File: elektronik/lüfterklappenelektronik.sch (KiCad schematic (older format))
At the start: 96 parts, among them J101 Conn_01x05_Male, J102 Ckmtw_2510S-2P, J103 Conn_LAN_ENC28J60, J104 USB_B_Micro, J105 #Stecker, J106 Ckmtw_2510S-2P, J107 Ckmtw_2510S-2P, J108 Ckmtw_2510S-2P, P101 PWR_BUS_CONN1, P102 #FAN_230VAC_Phase, P103 PressureSensor3, P104 PressureSensor1, P105 PressureSensor2, P109 PWR_BUS_CONN2, Q101 IRLR8743TRPBF, Q102 IRLR8743TRPBF, Q103 IRLR8743TRPBF, Q104 Q_NPN_Darlington_BEC, Q105 Q_NPN_Darlington_BEC, SW101 SW_Push, SW102 SW_Push, U101 Gabellichtschranke, U102 Gabellichtschranke, U103 Gabellichtschranke, U104 #ZG3NC-240B, U105 ESP32-WROOM-32E, U106 AMS1117-3.3, U107 CP2102N-A01-GQFN28

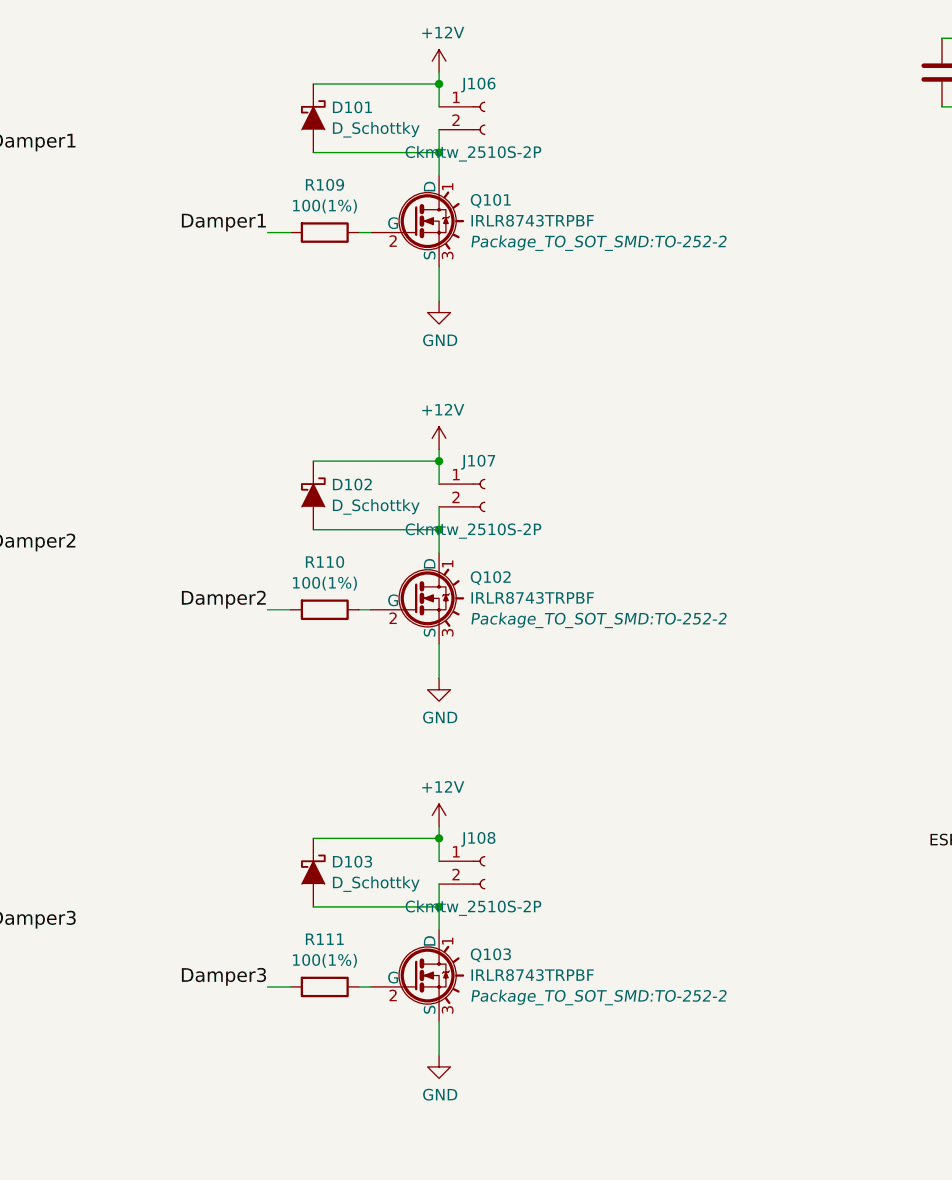
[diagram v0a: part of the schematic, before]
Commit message: place some groups
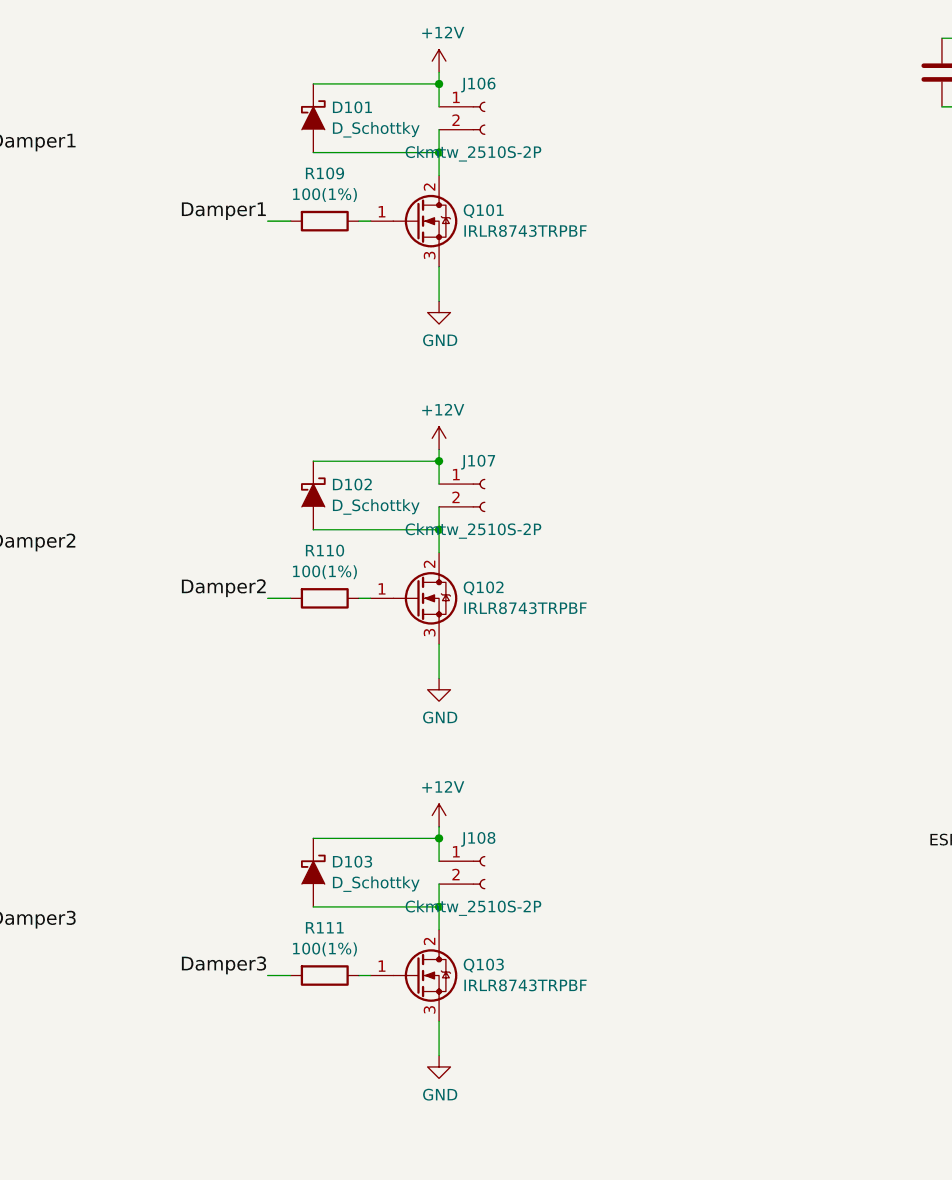
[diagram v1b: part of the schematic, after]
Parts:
- removed Q101, Q102, Q103: IRLR8743TRPBF, Package_TO_SOT_SMD:TO-252-2, symbol lüfterklappenelektronik-rescue:BUZ11
- added Q101, Q102, Q103: IRLR8743TRPBF, Package_TO_SOT_SMD:TO-252-2, symbol Transistor_FET:IRLB8721PBF
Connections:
- net GND: now also Q101.3 (S), Q102.3 (S), Q103.3 (S)
- net at D101.2 (A), J106.2 (Pin_2): now also Q101.2 (D)
- net at R109.1: now also Q101.1 (G)
- net at R110.1: now also Q102.1 (G)
- net at R111.1: now also Q103.1 (G)
- net at D103.2 (A), J108.2 (Pin_2): now also Q103.2 (D)
- net at D102.2 (A), J107.2 (Pin_2): now also Q102.2 (D)
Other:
- moved on the sheet: R109, R110, R111
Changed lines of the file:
@@
 L lüfterklappenelektronik-rescue:R R109
 U 1 1 57419FFE
-P 4450 1850
-F 0 "R109" V 4243 1850 50  0000 C CNN
-F 1 "100(1%)" V 4334 1850 50  0000 C CNN
-F 2 "Resistor_SMD:R_0603_1608Metric" V 4380 1850 50  0001 C CNN
-F 3 "" H 4450 1850 50  0000 C CNN
-	1    4450 1850
-	0    1    1    0
-$EndComp
-Wire Wire Line
-	4600 1850 4650 1850
+P 4450 1800
+F 0 "R109" V 4243 1800 50  0000 C CNN
+F 1 "100(1%)" V 4334 1800 50  0000 C CNN
+F 2 "Resistor_SMD:R_0603_1608Metric" V 4380 1800 50  0001 C CNN
+F 3 "" H 4450 1800 50  0000 C CNN
+	1    4450 1800
+	0    1    1    0
+$EndComp
+Wire Wire Line
+	4600 1800 4650 1800
 $Comp
 L power:GND #PWR02
@@
 	1    0    0    -1
 $EndComp
-Wire Wire Line
-	4950 2000 4950 2150
-Text Label 4200 1850 2    60   ~ 0
+Text Label 4200 1800 2    60   ~ 0
 Damper1
 Wire Wire Line
-	4200 1850 4300 1850
+	4200 1800 4300 1800
 $Comp
 L power:+12V #PWR03
@@
 L lüfterklappenelektronik-rescue:R R110
 U 1 1 5741A896
-P 4450 3500
-F 0 "R110" V 4243 3500 50  0000 C CNN
-F 1 "100(1%)" V 4334 3500 50  0000 C CNN
-F 2 "Resistor_SMD:R_0603_1608Metric" V 4380 3500 50  0001 C CNN
-F 3 "" H 4450 3500 50  0000 C CNN
-	1    4450 3500
-	0    1    1    0
-$EndComp
-Wire Wire Line
-	4600 3500 4650 3500
+P 4450 3450
+F 0 "R110" V 4243 3450 50  0000 C CNN
+F 1 "100(1%)" V 4334 3450 50  0000 C CNN
+F 2 "Resistor_SMD:R_0603_1608Metric" V 4380 3450 50  0001 C CNN
+F 3 "" H 4450 3450 50  0000 C CNN
+	1    4450 3450
+	0    1    1    0
+$EndComp
+Wire Wire Line
+	4600 3450 4650 3450
 $Comp
 L power:GND #PWR04
@@
 Wire Wire Line
 	4950 3650 4950 3800
-Text Label 4200 3500 2    60   ~ 0
+Text Label 4200 3450 2    60   ~ 0
 Damper2
 Wire Wire Line
-	4200 3500 4300 3500
+	4200 3450 4300 3450
 $Comp
 L power:+12V #PWR05
@@
 L lüfterklappenelektronik-rescue:R R111
 U 1 1 5741AA44
-P 4450 5150
-F 0 "R111" V 4243 5150 50  0000 C CNN
-F 1 "100(1%)" V 4334 5150 50  0000 C CNN
-F 2 "Resistor_SMD:R_0603_1608Metric" V 4380 5150 50  0001 C CNN
-F 3 "" H 4450 5150 50  0000 C CNN
-	1    4450 5150
-	0    1    1    0
-$EndComp
-Wire Wire Line
-	4600 5150 4650 5150
+P 4450 5100
+F 0 "R111" V 4243 5100 50  0000 C CNN
+F 1 "100(1%)" V 4334 5100 50  0000 C CNN
+F 2 "Resistor_SMD:R_0603_1608Metric" V 4380 5100 50  0001 C CNN
+F 3 "" H 4450 5100 50  0000 C CNN
+	1    4450 5100
+	0    1    1    0
+$EndComp
+Wire Wire Line
+	4600 5100 4650 5100
 $Comp
 L power:GND #PWR06
@@
 Wire Wire Line
 	4950 5300 4950 5450
-Text Label 4200 5150 2    60   ~ 0
+Text Label 4200 5100 2    60   ~ 0
 Damper3
 Wire Wire Line
-	4200 5150 4300 5150
+	4200 5100 4300 5100
 Text Label 3050 6750 2    60   ~ 0
 FAN
@@
 F 3 "" H 1950 6650 50  0000 C CNN
 	1    1950 6650
-	1    0    0    -1
-$EndComp
-$Comp
-L lüfterklappenelektronik-rescue:BUZ11 Q103
-U 1 1 57544167
-P 4850 5100
-F 0 "Q103" H 5085 5191 50  0000 L CNN
-F 1 "IRLR8743TRPBF" H 5085 5100 50  0000 L CNN
-F 2 "Package_TO_SOT_SMD:TO-252-2" H 5085 5009 50  0000 L CIN
-F 3 "" H 4850 5100 50  0000 L CNN
-	1    4850 5100
-	1    0    0    -1
-$EndComp
-$Comp
-L lüfterklappenelektronik-rescue:BUZ11 Q102
-U 1 1 5754473E
-P 4850 3450
-F 0 "Q102" H 5085 3541 50  0000 L CNN
-F 1 "IRLR8743TRPBF" H 5085 3450 50  0000 L CNN
-F 2 "Package_TO_SOT_SMD:TO-252-2" H 5085 3359 50  0000 L CIN
-F 3 "" H 4850 3450 50  0000 L CNN
-	1    4850 3450
-	1    0    0    -1
-$EndComp
-$Comp
-L lüfterklappenelektronik-rescue:BUZ11 Q101
-U 1 1 575449DD
-P 4850 1800
-F 0 "Q101" H 5085 1891 50  0000 L CNN
-F 1 "IRLR8743TRPBF" H 5085 1800 50  0000 L CNN
-F 2 "Package_TO_SOT_SMD:TO-252-2" H 5085 1709 50  0000 L CIN
-F 3 "https://datasheet.lcsc.com/szlcsc/1809061832_Infineon-Technologies-IRLR8743TRPBF_C51360.pdf" H 4850 1800 50  0001 L CNN
-F 4 "Infineon Technologies" H 4850 1800 50  0001 C CNN "MF"
-F 5 "IRLR8743TRPBF" H 4850 1800 50  0001 C CNN "MP"
-F 6 "LCSC" H 4850 1800 50  0001 C CNN "Distributor"
-F 7 "C51360" H 4850 1800 50  0001 C CNN "LCSCPartN"
-	1    4850 1800
 	1    0    0    -1
 $EndComp
@@
 	1    0    0    -1
 $EndComp
+$Comp
+L Transistor_FET:IRLB8721PBF Q101
+U 1 1 6113C9FF
+P 4850 1800
+F 0 "Q101" H 5054 1846 50  0000 L CNN
+F 1 "IRLR8743TRPBF" H 5054 1755 50  0000 L CNN
+F 2 "Package_TO_SOT_SMD:TO-252-2" H 5100 1725 50  0001 L CIN
+F 3 "https://datasheet.lcsc.com/szlcsc/1809061832_Infineon-Technologies-IRLR8743TRPBF_C51360.pdf" H 4850 1800 50  0001 L CNN
+F 4 "Infineon Technologies" H 4850 1800 50  0001 C CNN "MF"
+F 5 "IRLR8743TRPBF" H 4850 1800 50  0001 C CNN "MP"
+F 6 "LCSC" H 4850 1800 50  0001 C CNN "Distributor"
+F 7 "C51360" H 4850 1800 50  0001 C CNN "LCSCPartN"
+F 8 "SMT" H 4850 1800 50  0001 C CNN "Type"
+	1    4850 1800
+	1    0    0    -1
+$EndComp
+Wire Wire Line
+	4950 2000 4950 2150
+$Comp
+L Transistor_FET:IRLB8721PBF Q102
+U 1 1 6118E7D4
+P 4850 3450
+F 0 "Q102" H 5054 3496 50  0000 L CNN
+F 1 "IRLR8743TRPBF" H 5054 3405 50  0000 L CNN
+F 2 "Package_TO_SOT_SMD:TO-252-2" H 5100 3375 50  0001 L CIN
+F 3 "https://datasheet.lcsc.com/szlcsc/1809061832_Infineon-Technologies-IRLR8743TRPBF_C51360.pdf" H 4850 3450 50  0001 L CNN
+F 4 "Infineon Technologies" H 4850 3450 50  0001 C CNN "MF"
+F 5 "IRLR8743TRPBF" H 4850 3450 50  0001 C CNN "MP"
+F 6 "LCSC" H 4850 3450 50  0001 C CNN "Distributor"
+F 7 "C51360" H 4850 3450 50  0001 C CNN "LCSCPartN"
+F 8 "SMT" H 4850 3450 50  0001 C CNN "Type"
+	1    4850 3450
+	1    0    0    -1
+$EndComp
+$Comp
+L Transistor_FET:IRLB8721PBF Q103
+U 1 1 6118F713
+P 4850 5100
+F 0 "Q103" H 5054 5146 50  0000 L CNN
+F 1 "IRLR8743TRPBF" H 5054 5055 50  0000 L CNN
+F 2 "Package_TO_SOT_SMD:TO-252-2" H 5100 5025 50  0001 L CIN
+F 3 "https://datasheet.lcsc.com/szlcsc/1809061832_Infineon-Technologies-IRLR8743TRPBF_C51360.pdf" H 4850 5100 50  0001 L CNN
+F 4 "Infineon Technologies" H 4850 5100 50  0001 C CNN "MF"
+F 5 "IRLR8743TRPBF" H 4850 5100 50  0001 C CNN "MP"
+F 6 "LCSC" H 4850 5100 50  0001 C CNN "Distributor"
+F 7 "C51360" H 4850 5100 50  0001 C CNN "LCSCPartN"
+F 8 "SMT" H 4850 5100 50  0001 C CNN "Type"
+	1    4850 5100
+	1    0    0    -1
+$EndComp

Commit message: rough placing
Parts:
- J106, J107, J108: value Ckmtw_2510S-2P -> WJ2EDGRC-5.08-2P; footprint Connect:PINHEAD1-2 -> FootprintsTittelbach:WJ2EDGRC-5.08-2P; LCSCPartN C30436 -> C3697; MF BOOMELE(Boom Precision Elec) -> Ningbo Kangnex Elec; MP C30436 -> WJ2EDGRC-5.08-2P
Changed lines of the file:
@@
 F 1 "Gabellichtschranke" H 1750 2034 50  0000 C CNN
 F 2 "FootprintsTittelbach:Ckmtw_2510S-4P" H 1750 1700 50  0001 C CNN
-F 3 "https://datasheet.lcsc.com/szlcsc/1811061121_BOOMELE-Boom-Precision-Elec-C31753_C31753.pdf" H 1750 1700 50  0001 C CNN
+F 3 "https://datasheet.lcsc.com/szlcsc/1806151523_Ckmtw-Shenzhen-Cankemeng-2510S-4P_C140769.pdf" H 1750 1700 50  0001 C CNN
 F 4 "Ckmtw(Shenzhen Cankemeng)" H 1750 1700 50  0001 C CNN "MF"
 F 5 "2510S-4P" H 1750 1700 50  0001 C CNN "MP"
@@
 F 1 "Gabellichtschranke" H 1750 3784 50  0000 C CNN
 F 2 "FootprintsTittelbach:Ckmtw_2510S-4P" H 1750 3450 50  0001 C CNN
-F 3 "https://datasheet.lcsc.com/szlcsc/1811061121_BOOMELE-Boom-Precision-Elec-C31753_C31753.pdf" H 1750 3450 50  0001 C CNN
+F 3 "https://datasheet.lcsc.com/szlcsc/1806151523_Ckmtw-Shenzhen-Cankemeng-2510S-4P_C140769.pdf" H 1750 3450 50  0001 C CNN
 F 4 "Ckmtw(Shenzhen Cankemeng)" H 1750 3450 50  0001 C CNN "MF"
 F 5 "2510S-4P" H 1750 3450 50  0001 C CNN "MP"
@@
 F 1 "Gabellichtschranke" H 1750 5434 50  0000 C CNN
 F 2 "FootprintsTittelbach:Ckmtw_2510S-4P" H 1750 5100 50  0001 C CNN
-F 3 "https://datasheet.lcsc.com/szlcsc/1811061121_BOOMELE-Boom-Precision-Elec-C31753_C31753.pdf" H 1750 5100 50  0001 C CNN
+F 3 "https://datasheet.lcsc.com/szlcsc/1806151523_Ckmtw-Shenzhen-Cankemeng-2510S-4P_C140769.pdf" H 1750 5100 50  0001 C CNN
 F 4 "Ckmtw(Shenzhen Cankemeng)" H 1750 5100 50  0001 C CNN "MF"
 F 5 "2510S-4P" H 1750 5100 50  0001 C CNN "MP"
@@
 P 5150 1300
 F 0 "J106" H 5050 1400 50  0000 L CNN
-F 1 "Ckmtw_2510S-2P" H 4800 1100 50  0000 L CNN
-F 2 "Connect:PINHEAD1-2" H 5150 1300 50  0001 C CNN
-F 3 "~" H 5150 1300 50  0001 C CNN
-F 4 " BOOMELE(Boom Precision Elec) " H 5150 1300 50  0001 C CNN "MF"
-F 5 "C30436" H 5150 1300 50  0001 C CNN "MP"
+F 1 "WJ2EDGRC-5.08-2P" H 4800 1100 50  0000 L CNN
+F 2 "FootprintsTittelbach:WJ2EDGRC-5.08-2P" H 5150 1300 50  0001 C CNN
+F 3 "https://datasheet.lcsc.com/szlcsc/1912251631_Ningbo-Kangnex-Elec-WJ2EDGRC-5-08-2P_C3697.pdf" H 5150 1300 50  0001 C CNN
+F 4 "Ningbo Kangnex Elec" H 5150 1300 50  0001 C CNN "MF"
+F 5 "WJ2EDGRC-5.08-2P" H 5150 1300 50  0001 C CNN "MP"
 F 6 "LCSC" H 5150 1300 50  0001 C CNN "Distributor"
-F 7 "C30436" H 5150 1300 50  0001 C CNN "LCSCPartN"
+F 7 "C3697" H 5150 1300 50  0001 C CNN "LCSCPartN"
 	1    5150 1300
-	1    0    0    -1
-$EndComp
-$Comp
-L Connector:Conn_01x02_Female J107
-U 1 1 60FA2504
-P 5150 2950
-F 0 "J107" H 5050 3050 50  0000 L CNN
-F 1 "Ckmtw_2510S-2P" H 4800 2750 50  0000 L CNN
-F 2 "Connect:PINHEAD1-2" H 5150 2950 50  0001 C CNN
-F 3 "~" H 5150 2950 50  0001 C CNN
-F 4 " BOOMELE(Boom Precision Elec) " H 5150 2950 50  0001 C CNN "MF"
-F 5 "C30436" H 5150 2950 50  0001 C CNN "MP"
-F 6 "LCSC" H 5150 2950 50  0001 C CNN "Distributor"
-F 7 "C30436" H 5150 2950 50  0001 C CNN "LCSCPartN"
-	1    5150 2950
-	1    0    0    -1
-$EndComp
-$Comp
-L Connector:Conn_01x02_Female J108
-U 1 1 60FA3064
-P 5150 4600
-F 0 "J108" H 5050 4700 50  0000 L CNN
-F 1 "Ckmtw_2510S-2P" H 4800 4400 50  0000 L CNN
-F 2 "Connect:PINHEAD1-2" H 5150 4600 50  0001 C CNN
-F 3 "~" H 5150 4600 50  0001 C CNN
-F 4 " BOOMELE(Boom Precision Elec) " H 5150 4600 50  0001 C CNN "MF"
-F 5 "C30436" H 5150 4600 50  0001 C CNN "MP"
-F 6 "LCSC" H 5150 4600 50  0001 C CNN "Distributor"
-F 7 "C30436" H 5150 4600 50  0001 C CNN "LCSCPartN"
-	1    5150 4600
 	1    0    0    -1
 $EndComp
@@
 	1    0    0    -1
 $EndComp
+$Comp
+L Connector:Conn_01x02_Female J107
+U 1 1 5FB0C768
+P 5150 2950
+F 0 "J107" H 5050 3050 50  0000 L CNN
+F 1 "WJ2EDGRC-5.08-2P" H 4800 2750 50  0000 L CNN
+F 2 "FootprintsTittelbach:WJ2EDGRC-5.08-2P" H 5150 2950 50  0001 C CNN
+F 3 "https://datasheet.lcsc.com/szlcsc/1912251631_Ningbo-Kangnex-Elec-WJ2EDGRC-5-08-2P_C3697.pdf" H 5150 2950 50  0001 C CNN
+F 4 "Ningbo Kangnex Elec" H 5150 2950 50  0001 C CNN "MF"
+F 5 "WJ2EDGRC-5.08-2P" H 5150 2950 50  0001 C CNN "MP"
+F 6 "LCSC" H 5150 2950 50  0001 C CNN "Distributor"
+F 7 "C3697" H 5150 2950 50  0001 C CNN "LCSCPartN"
+	1    5150 2950
+	1    0    0    -1
+$EndComp
+$Comp
+L Connector:Conn_01x02_Female J108
+U 1 1 5FB0D4B1
+P 5150 4600
+F 0 "J108" H 5050 4700 50  0000 L CNN
+F 1 "WJ2EDGRC-5.08-2P" H 4800 4400 50  0000 L CNN
+F 2 "FootprintsTittelbach:WJ2EDGRC-5.08-2P" H 5150 4600 50  0001 C CNN
+F 3 "https://datasheet.lcsc.com/szlcsc/1912251631_Ningbo-Kangnex-Elec-WJ2EDGRC-5-08-2P_C3697.pdf" H 5150 4600 50  0001 C CNN
+F 4 "Ningbo Kangnex Elec" H 5150 4600 50  0001 C CNN "MF"
+F 5 "WJ2EDGRC-5.08-2P" H 5150 4600 50  0001 C CNN "MP"
+F 6 "LCSC" H 5150 4600 50  0001 C CNN "Distributor"
+F 7 "C3697" H 5150 4600 50  0001 C CNN "LCSCPartN"
+	1    5150 4600
+	1    0    0    -1
+$EndComp

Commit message: added more noise and transient protection
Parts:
- added C116, C117, C118, C119, C120, C121, C122, C123, C124: 100P, Capacitor_SMD:C_0603_1608Metric, symbol Device:C
- added L101, L102, L103, L104, L105, L106, L107, L108, L109, L110, L111: GZ1608D222TF, Inductor_SMD:L_0603_1608Metric_Pad1.05x0.95mm_HandSolder, symbol Device:L_Core_Ferrite_Small
- added R132, R133: 5K6(1%), Resistor_SMD:R_0603_1608Metric, symbol Device:R
- added R134: 10K(5%), Resistor_SMD:R_0603_1608Metric, symbol Device:R
- R101, R102, R103: value 43(1%) -> 91(1%)
- R104, R105, R106: value 2K2 -> 5K6(1%)
- R109, R110, R111: value 100(1%) -> 91(1%)
- R118, R119, R120, R121: value 22(1%) -> 220(1%)
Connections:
- net +3V3: now also C122.1, C123.1, C124.1, L107.2, L108.2, L109.2, R132.1, R133.1; no longer P103.1 (P1), P104.1 (P1), P105.1 (P1)
- net EndstopDamper1: now also R104.1; no longer D106.2 (A)
- net EndstopDamper2: now also R105.1; no longer D107.2 (A)
- net EndstopDamper3: now also R106.1; no longer D108.2 (A)
- net FAN: now also U105.9 (IO33); no longer U105.10 (IO25)
- net GND: now also U101.4 (Rl), U102.4 (Rl), U103.4 (Rl), C116.2, C117.2, C118.2, C119.2, C120.2, C121.2, C122.2, C123.2, C124.2, R134.2; no longer R104.2, R105.2, R106.2
- net PJON: now also L111.1; no longer R118.2
- net at D104.1 (A1), R107.1: now also L110.2; no longer J102.2 (Pin_2)
- net at U101.1 (A): now also L101.1; no longer R101.2
- net at U101.3 (Rh): now also L104.2; no longer D106.1 (K)
- net at R102.2: now also C117.1, L102.2; no longer U102.1 (A)
- net at R103.2: now also C118.1, L103.2; no longer U103.1 (A)
- net at R118.1: now also U105.10 (IO25); no longer U105.9 (IO33)
- net at D107.1 (K): now also C119.1, L105.1; no longer U102.3 (Rh)
- net at D108.1 (K): now also C120.1, L106.1; no longer U103.3 (Rh)
- new net: C116.1, L101.2, R101.2
- new net: D106.2 (A), R104.2
- new net: D107.2 (A), R105.2, R132.2
- new net: D108.2 (A), R106.2, R133.2
- new net: L109.1, P103.1 (P1)
- new net: L108.1, P105.1 (P1)
- new net: L107.1, P104.1 (P1)
- new net: L111.2, R118.2, R134.1
- new net: J102.2 (Pin_2), L110.1
- new net: C121.1, D106.1 (K), L104.1
- new net: L105.2, U102.3 (Rh)
- new net: L106.2, U103.3 (Rh)
- new net: L102.1, U102.1 (A)
- new net: L103.1, U103.1 (A)
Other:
- note added: "20mA"
- note removed: "37..42mA"
- note removed: "Widerstände schon auf Gabellichtschranke???"
- moved on the sheet: D101, D102, D103, D104, D106, D107, D108, J106, J107, J108, Q101, Q102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

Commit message: placing mostly done
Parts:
- removed C123, C124: 100P, Capacitor_SMD:C_0603_1608Metric, symbol Device:C
- removed L108, L109: GZ1608D222TF, Inductor_SMD:L_0603_1608Metric_Pad1.05x0.95mm_HandSolder, symbol Device:L_Core_Ferrite_Small
- added C125, C126, C127, C128, C129: 100P, Capacitor_SMD:C_0603_1608Metric, symbol Device:C
- added R135: 5K6(1%), Resistor_SMD:R_0603_1608Metric, symbol Device:R
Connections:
- net +3V3: now also R135.1
- net GND: now also D104.1 (A1), C125.2, C126.2, C127.2, C128.2, C129.2; no longer D104.2 (A2)
- net at L110.2, R107.1: now also C128.1; no longer D104.1 (A1)
- net at L104.2, U101.3 (Rh): now also C125.1
- net at D106.2 (A), R104.2: now also R135.2
- net at P103.1 (P1): now also L107.1, P104.1 (P1), P105.1 (P1)
- net at J102.2 (Pin_2), L110.1: now also D104.2 (A2), C129.1
- net at L105.2, U102.3 (Rh): now also C126.1
- net at L106.2, U103.3 (Rh): now also C127.1
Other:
- note added: "CLC π-Filter for Signal"
- note added: "LC Filter for current suppyl"
- moved on the sheet: C119, C120, C121, D104, D106, D107, D108, L104, L105, L106, L107, L110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
